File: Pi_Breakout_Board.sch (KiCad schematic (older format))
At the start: 74 parts, among them J1 Raspberry_Pi_2_3, J2 Conn_02x04_Odd_Even heater he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, J3 Conn_02x08_Odd_Even thermisto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, J4 Screw_Terminal_01x02, J5 Conn_01x08_Male, J6 Conn_01x08_Male, J7 Conn_01x02_Female, J8 Conn_01x03_Male, Q1 Q_NMOS_GDSD, Q2 Q_NMOS_GDSD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

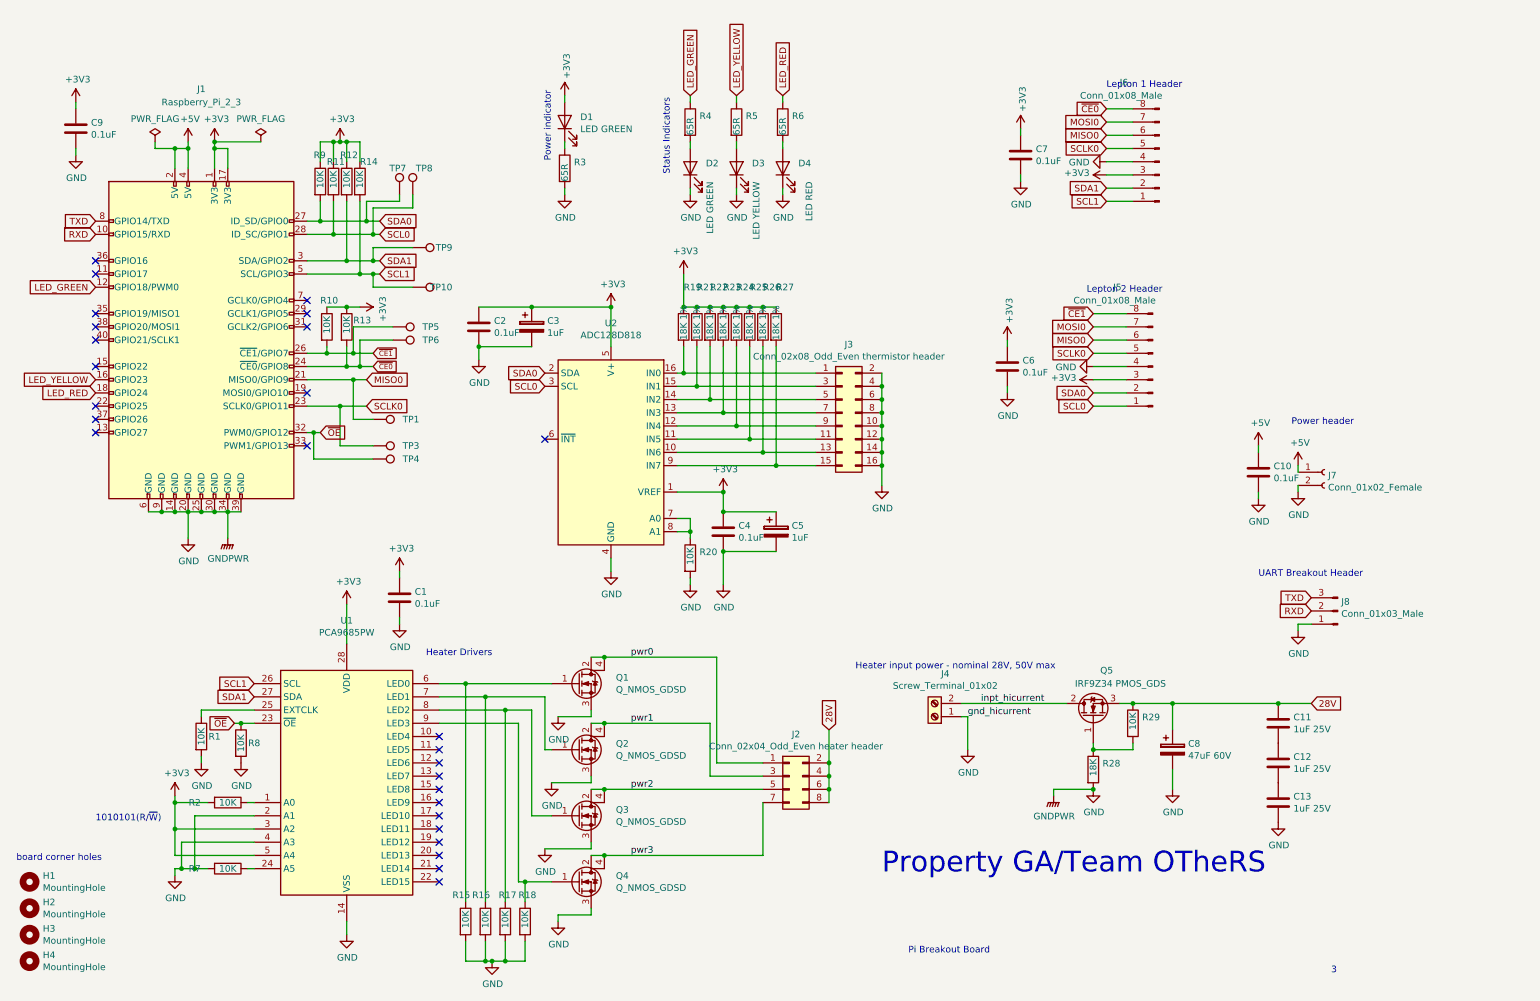
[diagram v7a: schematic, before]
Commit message: Renaming + minor revs. Ready for spin 2
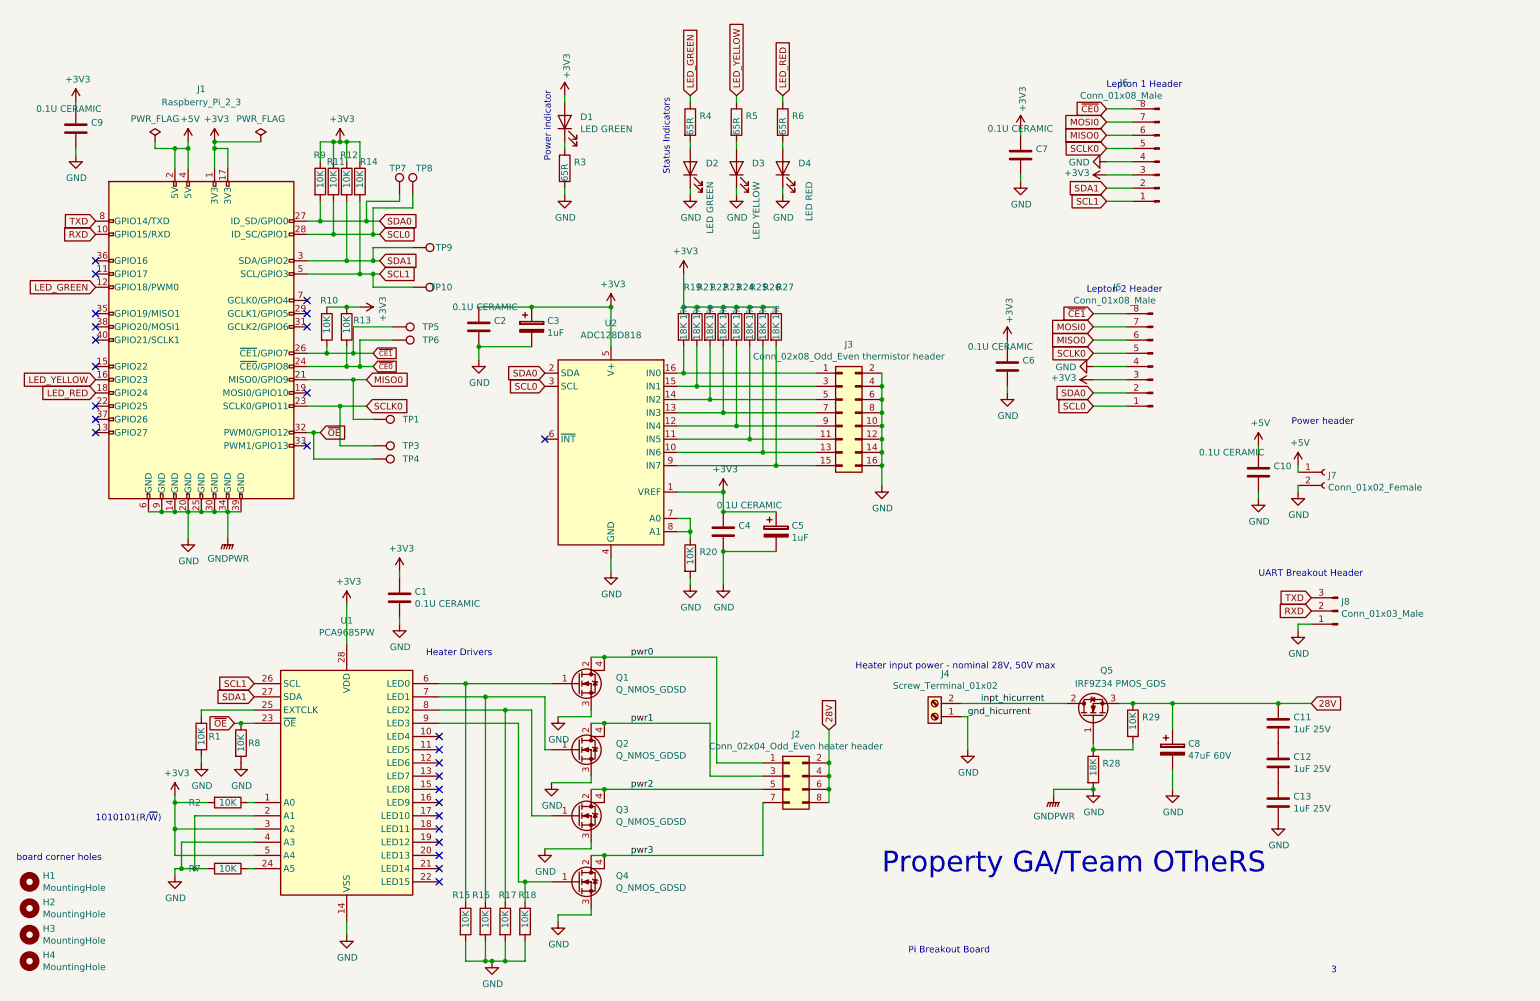
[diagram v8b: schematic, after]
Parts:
- C1, C10, C2, C4, C6, C7, C9: value 0.1uF -> 0.1U CERAMIC
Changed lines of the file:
@@
 P 3550 4800
 F 0 "C1" H 3665 4846 50  0000 L CNN
-F 1 "0.1uF" H 3665 4755 50  0000 L CNN
+F 1 "0.1U CERAMIC" H 3665 4755 50  0000 L CNN
 F 2 "Capacitor_SMD:C_1210_3225Metric_Pad1.42x2.65mm_HandSolder" H 3588 4650 50  0001 C CNN
 F 3 "~" H 3550 4800 50  0001 C CNN
@@
 P 10050 3850
 F 0 "C10" H 10165 3896 50  0000 L CNN
-F 1 "0.1uF" H 10165 3805 50  0000 L CNN
+F 1 "0.1U CERAMIC" H 9600 4000 50  0000 L CNN
 F 2 "Capacitor_SMD:C_1210_3225Metric_Pad1.42x2.65mm_HandSolder" H 10088 3700 50  0001 C CNN
 F 3 "~" H 10050 3850 50  0001 C CNN
@@
 P 8150 3050
 F 0 "C6" H 8265 3096 50  0000 L CNN
-F 1 "0.1uF" H 8265 3005 50  0000 L CNN
+F 1 "0.1U CERAMIC" H 7850 3200 50  0000 L CNN
 F 2 "Capacitor_SMD:C_1210_3225Metric_Pad1.42x2.65mm_HandSolder" H 8188 2900 50  0001 C CNN
 F 3 "~" H 8150 3050 50  0001 C CNN
@@
 P 8250 1450
 F 0 "C7" H 8365 1496 50  0000 L CNN
-F 1 "0.1uF" H 8365 1405 50  0000 L CNN
+F 1 "0.1U CERAMIC" H 8000 1650 50  0000 L CNN
 F 2 "Capacitor_SMD:C_1210_3225Metric_Pad1.42x2.65mm_HandSolder" H 8288 1300 50  0001 C CNN
 F 3 "~" H 8250 1450 50  0001 C CNN
@@
 P 6000 4300
 F 0 "C4" H 6115 4346 50  0000 L CNN
-F 1 "0.1uF" H 6115 4255 50  0000 L CNN
+F 1 "0.1U CERAMIC" H 5950 4500 50  0000 L CNN
 F 2 "Capacitor_SMD:C_1210_3225Metric_Pad1.42x2.65mm_HandSolder" H 6038 4150 50  0001 C CNN
 F 3 "~" H 6000 4300 50  0001 C CNN
@@
 P 4150 2750
 F 0 "C2" H 4265 2796 50  0000 L CNN
-F 1 "0.1uF" H 4265 2705 50  0000 L CNN
+F 1 "0.1U CERAMIC" H 3950 2900 50  0000 L CNN
 F 2 "Capacitor_SMD:C_1210_3225Metric_Pad1.42x2.65mm_HandSolder" H 4188 2600 50  0001 C CNN
 F 3 "~" H 4150 2750 50  0001 C CNN
@@
 P 1100 1250
 F 0 "C9" H 1215 1296 50  0000 L CNN
-F 1 "0.1uF" H 1215 1205 50  0000 L CNN
+F 1 "0.1U CERAMIC" H 800 1400 50  0000 L CNN
 F 2 "Capacitor_SMD:C_1210_3225Metric_Pad1.42x2.65mm_HandSolder" H 1138 1100 50  0001 C CNN
 F 3 "~" H 1100 1250 50  0001 C CNN
